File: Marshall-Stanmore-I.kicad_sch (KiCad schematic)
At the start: 64 parts, among them Q1 MPSW42, Q7 FDPF10N60NZ, T1 TRISTAR13030122, U1 OB2269, U2 FAN431A, U5 LM317, U9 EL817

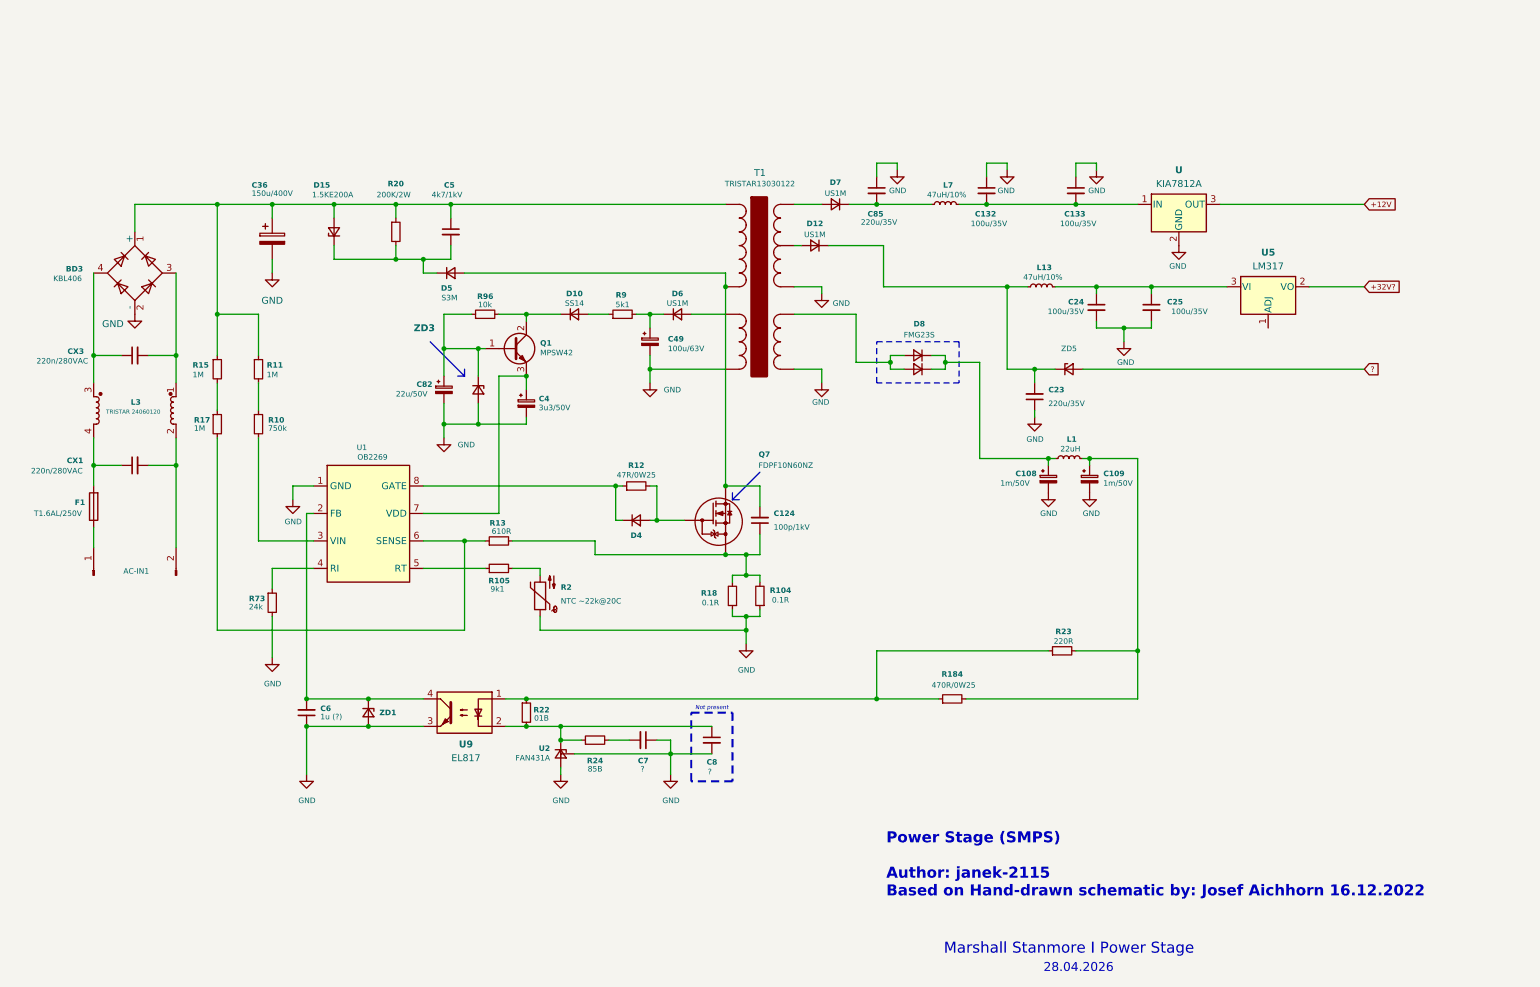
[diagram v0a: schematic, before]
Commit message: Added a missing part of the original schematic (left side), rearranged the components a little bit for better clarity, marked the 4 diodes making up the bridge rectifier are a single package.
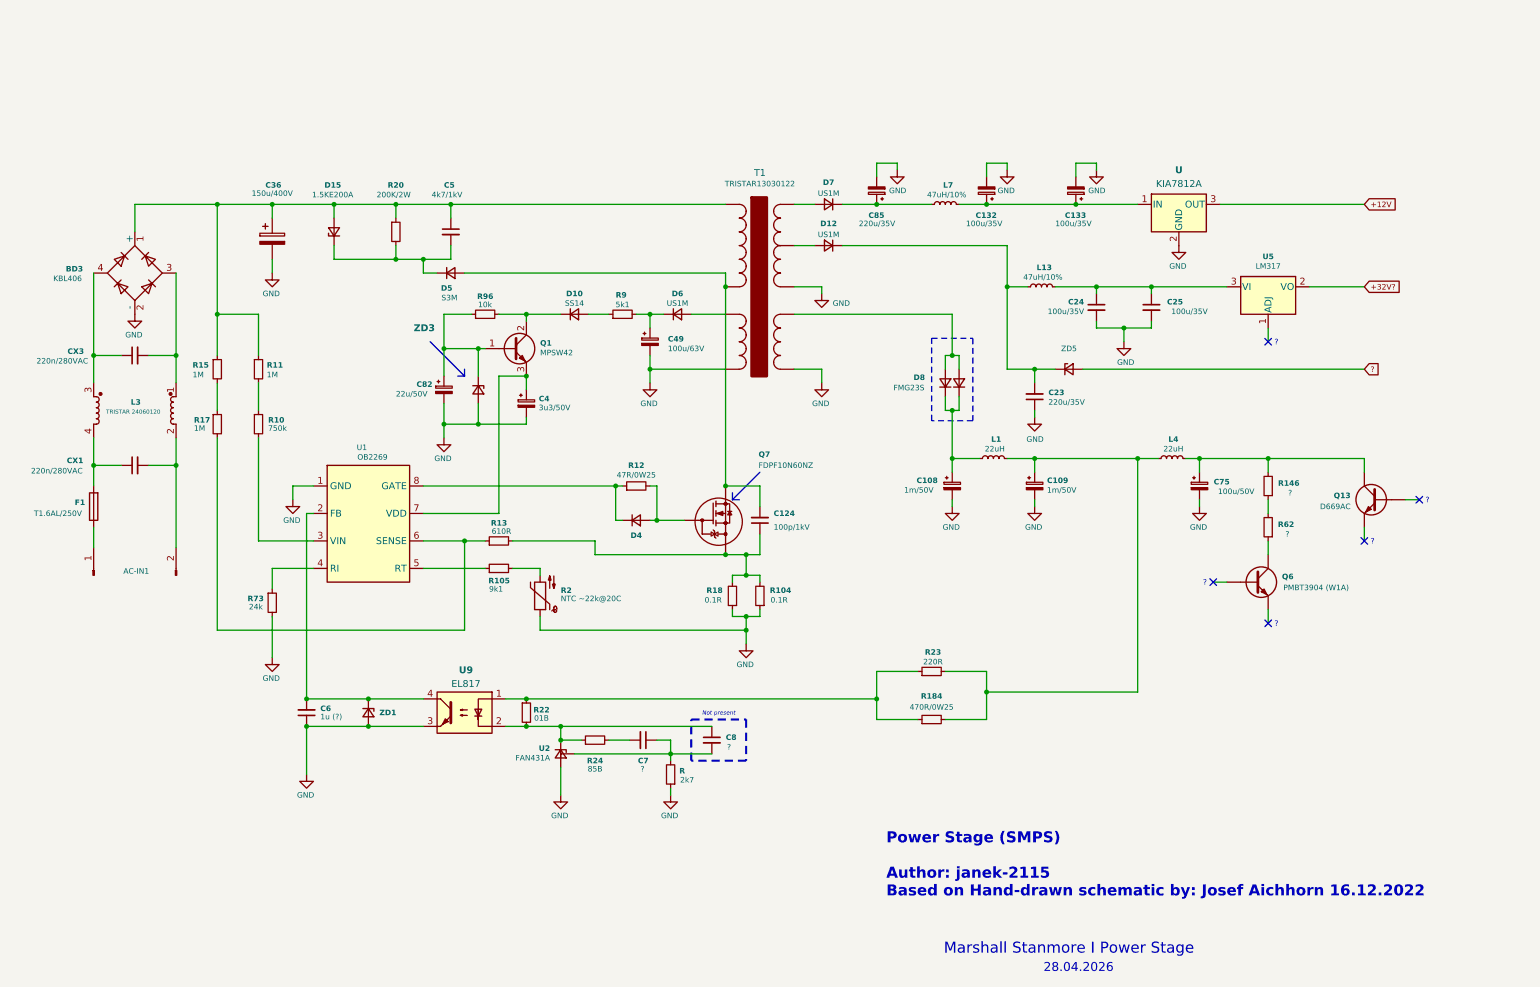
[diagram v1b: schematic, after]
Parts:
- added C75: 100u/50V, symbol Device:C_Polarized_Small
- added L4: 22uH, symbol Device:L_Small
- added Q13: D669AC, symbol Device:Q_NPN
- added Q6: PMBT3904 (W1A), symbol Device:Q_NPN
- added R: 2k7, symbol Device:R_Small
- added R146, R62: ?, symbol Device:R_Small
- C132, C133, C85: symbol Device:C_Small -> Device:C_Polarized_Small
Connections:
- net GND: now also C132.2, C133.2, C85.2, C75.2, R.1; no longer C132.1, C133.1, C7.1, C8.2, C85.1, U2.3 (REF)
- net at L7.2, U.1 (IN): now also C132.1, C133.1; no longer C132.2, C133.2
- net at D7.1 (K), L7.1: now also C85.1; no longer C85.2
- net at C109.1, L1.2, R184.2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: now also L4.1
- new net: C75.1, L4.2, Q13.C, R146.2
- new net: R146.1, R62.2
- new net: Q6.C, R62.1
- new net: C7.1, C8.2, R.2, U2.3 (REF)
- no-connect marks 0 -> 5
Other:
- note added: "?"
- moved on the sheet: C108, C109, D12, D7, D8, L1, R184, R23

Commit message: Added missing values for C6 and C7. Started working on the schematic of the audio output stage of the board. Made the schematic hierarchical. Added .png of the new audio output stage schematic.
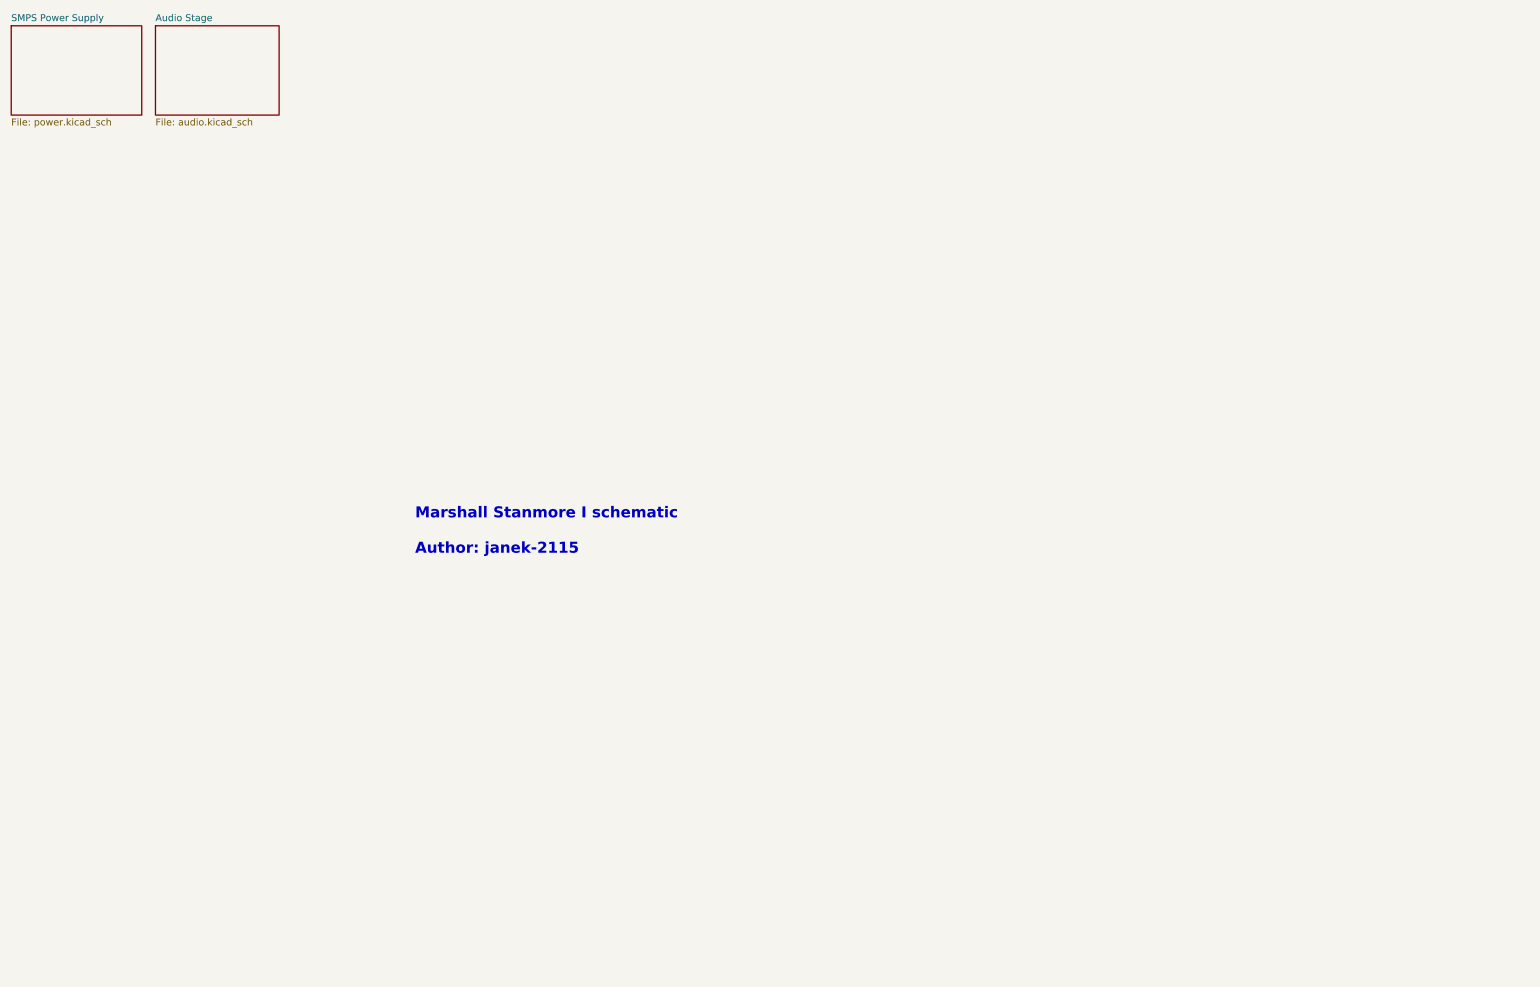
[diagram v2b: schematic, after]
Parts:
- removed AC-IN1: AC-IN1, symbol Connector:Conn_01x02_Pin
- removed BD3: KBL406, Diode_SMD:Diode_Bridge_Diotec_ABS, symbol Diode_Bridge:ABS2
- removed C108, C109: 1m/50V, symbol Device:C_Polarized_Small
- removed C124: 100p/1kV, symbol Device:C_Small
- removed C132, C133: 100u/35V, symbol Device:C_Polarized_Small
- removed C23: 220u/35V, symbol Device:C_Small
- removed C24, C25: 100u/35V, symbol Device:C_Small
- removed C36: 150u/400V, symbol Device:C_Polarized
- removed C4: 3u3/50V, symbol Device:C_Polarized_Small
- removed C49: 100u/63V, symbol Device:C_Polarized_Small
- removed C5: 4k7/1kV, symbol Device:C_Small
- removed C6: 1u (?), symbol Device:C_Small
- removed C7, C8: ?, symbol Device:C_Small
- removed C75: 100u/50V, symbol Device:C_Polarized_Small
- removed C82: 22u/50V, symbol Device:C_Polarized_Small
- removed C85: 220u/35V, symbol Device:C_Polarized_Small
- removed CX1, CX3: 220n/280VAC, symbol Device:C_Small
- removed D10: SS14, symbol Device:D_Small
- removed D12, D6, D7, D8: US1M, symbol Device:D_Small
- removed D15: 1.5KE200A, Diode_THT:D_DO-201AE_P15.24mm_Horizontal, symbol Device:D_Zener_Small
- removed D4: ~, symbol Device:D_Small
- removed D5: S3M, symbol Device:D_Small
- removed D8: FMG23S, symbol Device:D_Small
- removed F1: T1.6AL/250V, symbol Device:Fuse
- removed L1, L4: 22uH, symbol Device:L_Small
- removed L13, L7: 47uH/10%, symbol Device:L_Small
- removed L3: TRISTAR 24060120, symbol Device:L_Coupled
- removed Q1: MPSW42, Package_TO_SOT_THT:TO-92, symbol Transistor_BJT:Q_NPN_BCE
- removed Q13: D669AC, symbol Device:Q_NPN
- removed Q6: PMBT3904 (W1A), symbol Device:Q_NPN
- removed Q7: FDPF10N60NZ, Package_TO_SOT_THT:TO-220F-3_Vertical, symbol Device:Q_NMOS
- removed R: 2k7, symbol Device:R_Small
- removed R10: 750k, symbol Device:R_Small
- removed R104, R18: 0.1R, symbol Device:R_Small
- removed R105: 9k1, symbol Device:R_Small
- removed R11, R15, R17: 1M, symbol Device:R_Small
- removed R12: 47R/0W25, symbol Device:R_Small
- removed R13: 610R, symbol Device:R_Small
- removed R146, R62: ?, symbol Device:R_Small
- removed R184: 470R/0W25, symbol Device:R_Small
- removed R2: NTC ~22k@20C, symbol Device:Thermistor_NTC
- removed R20: 200K/2W, symbol Device:R_Small
- removed R22: 01B, symbol Device:R_Small
- removed R23: 220R, symbol Device:R_Small
- removed R24: 85B, symbol Device:R_Small
- removed R73: 24k, symbol Device:R_Small
- removed R9: 5k1, symbol Device:R_Small
- removed R96: 10k, symbol Device:R_Small
- removed T1: TRISTAR13030122, symbol Transformer:TRANSF6
- removed U: KIA7812A, symbol Regulator_Linear:L7812
- removed U1: OB2269, Package_SO:SOIC-8_3.9x4.9mm_P1.27mm, symbol Memory_RAM:ESP-PSRAM32
- removed U2: FAN431A, Package_TO_SOT_THT:TO-92, symbol Device:D_Zener_Small
- removed U5: LM317, Package_TO_SOT_THT:TO-220-3_Vertical, symbol Regulator_Linear:LM317_TO-220
- removed U9: EL817, symbol Isolator:Optocoupler_DC_PhotoNPN_AKEC
- removed ZD1, ZD3, ZD5: ~, symbol Device:D_Zener_Small
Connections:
- no-connect marks 5 -> 0
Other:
- added sheet Audio Stage (audio.kicad_sch)
- added sheet SMPS Power Supply (power.kicad_sch)
- note added: "Marshall Stanmore I schematic Author: janek-2115"
- note removed: "28.04.2026"
- note removed: "?"
- note removed: "Marshall Stanmore I Power Stage"
- note removed: "Not present"
- note removed: "Power Stage (SMPS) Author: janek-2115 Based on Hand-drawn schematic by: Josef Aichhorn 16.12.2022"
- title: (none) -> Marshall Stanmore I Main Page
